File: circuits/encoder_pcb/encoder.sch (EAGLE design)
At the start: 15 parts, among them U1 MPU-6050, U2 DS18B20, X1 0.5G-WTX-NPH

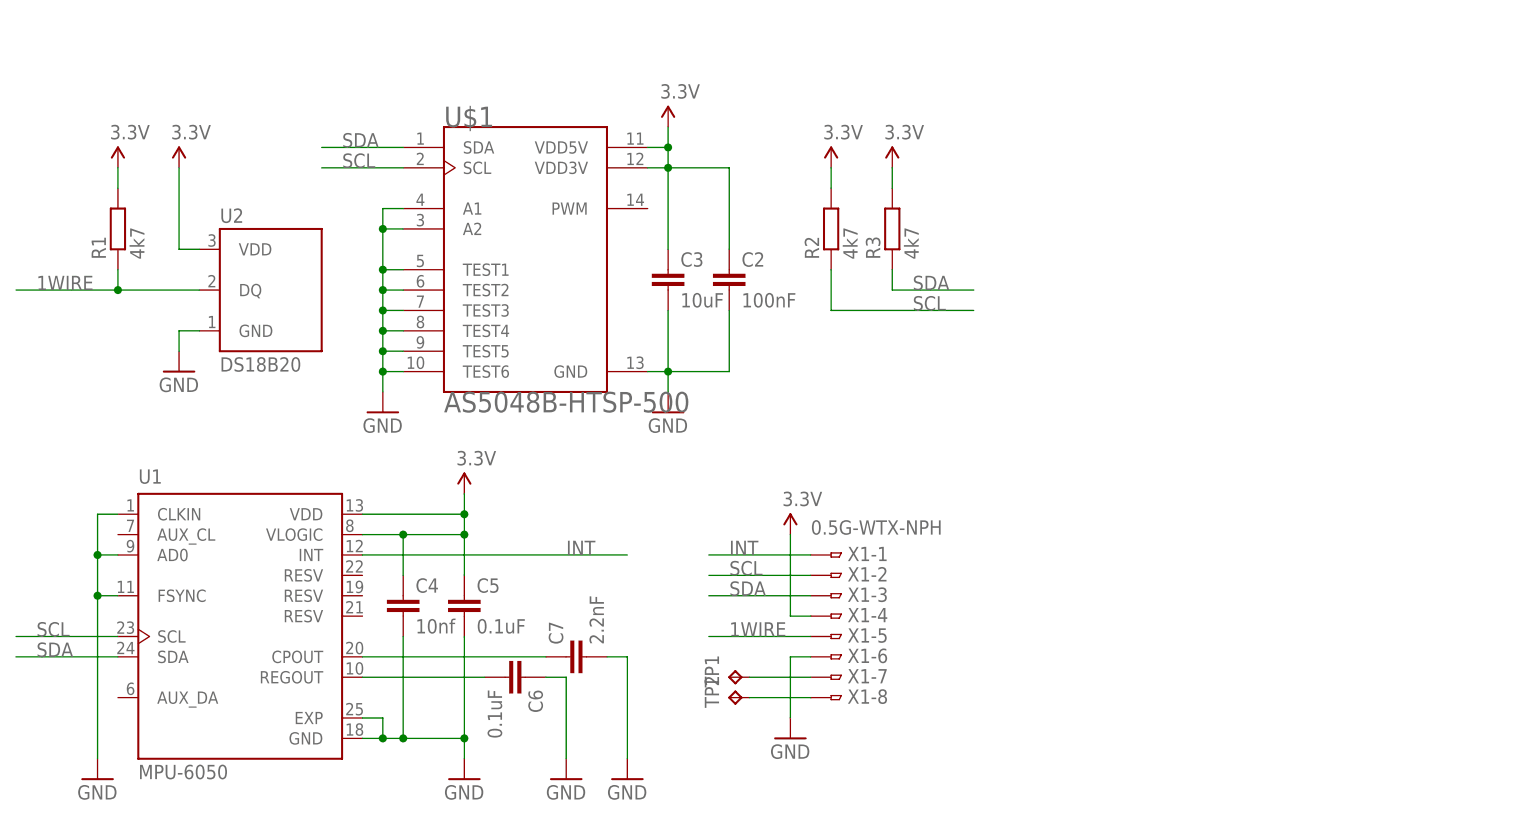
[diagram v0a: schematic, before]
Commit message: Updated encoder PCB - UNTESTED
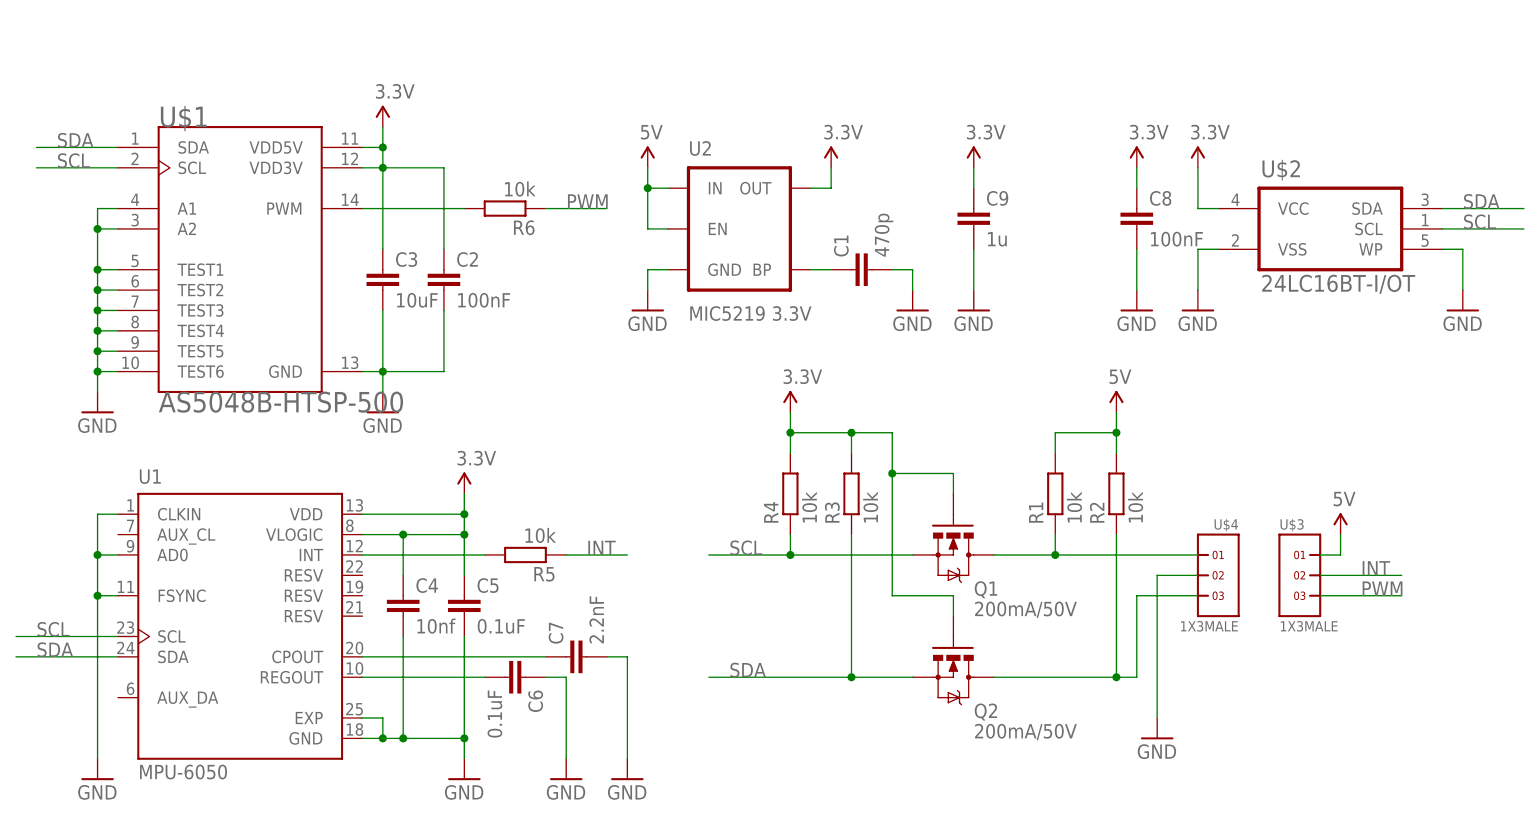
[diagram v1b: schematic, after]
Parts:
- removed TP1, TP2: TPB1,27, testpad:TPB1,27
- removed X1: 0.5G-WTX-NPH, FPC_connector_0.5G-WTX-nP:0.5G-WTX-NPH
- added C1: 470p, rcl:C-EUC0402K
- added C8: 100nF, rcl:C-EUC0402K
- added C9: 1u, rcl:C-EUC0402K
- added Q1, Q2: 200mA/50V, SparkFun-DiscreteSemi:MOSFET-NCHANNELBSS138
- added R4, R5, R6: 10k, rcl:R-EU_R0402
- added U$2: 24LC16BT-I/OT, 24LC16BT-I_OT:24LC16BT-I/OT
- added U$3, U$4: 1X3MALE, headers(.05in):1X3MALE
- R1, R2, R3: value 4k7 -> 10k
- U2: value DS18B20 -> MIC5219 3.3V; device SparkFun-Sensors:DS18B20 -> SparkFun-PowerIC:V_REG_MIC52193.3V
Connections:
- removed net 1WIRE: R1.1, U2.DQ, X1-5.1
- new net 5V: R1.2, R2.2, U$3.1, U2.EN, U2.IN
- new net N$5: R6.2, U$1.PWM
- new net N$6: Q1.D, R1.1, U$4.1
- new net N$7: Q2.D, R2.1, U$4.3
- new net PWM: R6.1, U$3.3
- net 3.3V: now also C8.1, C9.1, Q1.G, Q2.G, R4.2, U$2.VCC, U2.OUT; no longer R1.2, R2.2, U2.VDD, X1-4.1
- net GND: now also C1.2, C8.2, C9.2, U$2.VSS, U$2.WP, U$4.2; no longer X1-6.1
- net INT: now also R5.1, U$3.2; no longer U1.INT, X1-1.1
- net N$1: now also C1.1, U2.BP; no longer TP1.TP, X1-7.1
- net N$3: now also R5.2, U1.INT; no longer TP2.TP, X1-8.1
- net SCL: now also Q1.S, R4.1, U$2.SCL; no longer R2.1, X1-2.1
- net SDA: now also Q2.S, U$2.SDA; no longer X1-3.1
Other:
- moved on the sheet: C2, C3, R1, R2, R3, U$1

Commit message: Updated encoder board - UNTESTED
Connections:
- net N$6 renamed SCL_
- net N$7 renamed SDA_
- net 5V: now also U$3.3; no longer U$3.1
- net INT: now also U$3.1; no longer U$3.2
- net PWM: now also U$3.2; no longer U$3.3
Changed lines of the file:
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@@
 <net name="INT" class="0">
-<segment>
-<pinref part="U$3" gate="G$1" pin="2"/>
-<wire x1="127" y1="58.42" x2="137.16" y2="58.42" width="0.1524" layer="91"/>
-<label x="132.08" y="58.42" size="1.778" layer="95"/>
-</segment>
 <segment>
 <pinref part="R5" gate="G$1" pin="1"/>
 <wire x1="33.02" y1="60.96" x2="40.64" y2="60.96" width="0.1524" layer="91"/>
 <label x="35.56" y="60.96" size="1.778" layer="95"/>
+</segment>
+<segment>
+<pinref part="U$3" gate="G$1" pin="1"/>
+<wire x1="127" y1="60.96" x2="139.7" y2="60.96" width="0.1524" layer="91"/>
+<label x="132.08" y="60.96" size="1.778" layer="95"/>
 </segment>
 </net>
@@
 <net name="PWM" class="0">
 <segment>
-<pinref part="U$3" gate="G$1" pin="3"/>
-<wire x1="127" y1="55.88" x2="137.16" y2="55.88" width="0.1524" layer="91"/>
-<label x="132.08" y="55.88" size="1.778" layer="95"/>
-</segment>
-<segment>
 <pinref part="R6" gate="G$1" pin="1"/>
 <wire x1="30.48" y1="104.14" x2="38.1" y2="104.14" width="0.1524" layer="91"/>
 <label x="33.02" y="104.14" size="1.778" layer="95"/>
+</segment>
+<segment>
+<pinref part="U$3" gate="G$1" pin="2"/>
+<wire x1="127" y1="58.42" x2="139.7" y2="58.42" width="0.1524" layer="91"/>
+<label x="132.08" y="58.42" size="1.778" layer="95"/>
 </segment>
 </net>
@@
 </segment>
 <segment>
-<pinref part="U$3" gate="G$1" pin="1"/>
+<pinref part="U$3" gate="G$1" pin="3"/>
 <pinref part="SUPPLY2" gate="G$1" pin="5V"/>
-<wire x1="127" y1="60.96" x2="129.54" y2="60.96" width="0.1524" layer="91"/>
-<wire x1="129.54" y1="60.96" x2="129.54" y2="63.5" width="0.1524" layer="91"/>
+<wire x1="127" y1="55.88" x2="129.54" y2="55.88" width="0.1524" layer="91"/>
+<wire x1="129.54" y1="55.88" x2="129.54" y2="63.5" width="0.1524" layer="91"/>
 </segment>
 </net>
@@
 </segment>
 </net>
-<net name="N$6" class="0">
+<net name="SCL_" class="0">
 <segment>
 <pinref part="Q1" gate="G$1" pin="D"/>
@@
 <pinref part="R1" gate="G$1" pin="1"/>
 <wire x1="93.98" y1="63.5" x2="93.98" y2="60.96" width="0.1524" layer="91"/>
+<wire x1="93.98" y1="60.96" x2="111.76" y2="60.96" width="0.1524" layer="91"/>
+<junction x="93.98" y="60.96"/>
 <pinref part="U$4" gate="G$1" pin="1"/>
-<wire x1="111.76" y1="60.96" x2="93.98" y2="60.96" width="0.1524" layer="91"/>
-<junction x="93.98" y="60.96"/>
 </segment>
 </net>
-<net name="N$7" class="0">
+<net name="SDA_" class="0">
 <segment>
 <pinref part="Q2" gate="G$1" pin="D"/>

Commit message: Updated encoder to revision 1 - UNTESTED
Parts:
- removed R6: 10k, rcl:R-EU_R0402
- removed U$3, U$4: 1X3MALE, headers(.05in):1X3MALE
- added U$5: 1X5, headers(.05in):1X5
- renumbered U$1 to U4, U$2 to U3
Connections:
- removed net N$5: R6.2, U4.PWM
- removed net PWM: R6.1, U$3.2
- net 5V: now also U$5.2; no longer U$3.3
- net GND: now also U$5.4; no longer U$4.2
- net INT: now also U$5.1; no longer U$3.1
- net SCL_: now also U$5.5; no longer U$4.1
- net SDA_: now also U$5.3; no longer U$4.3

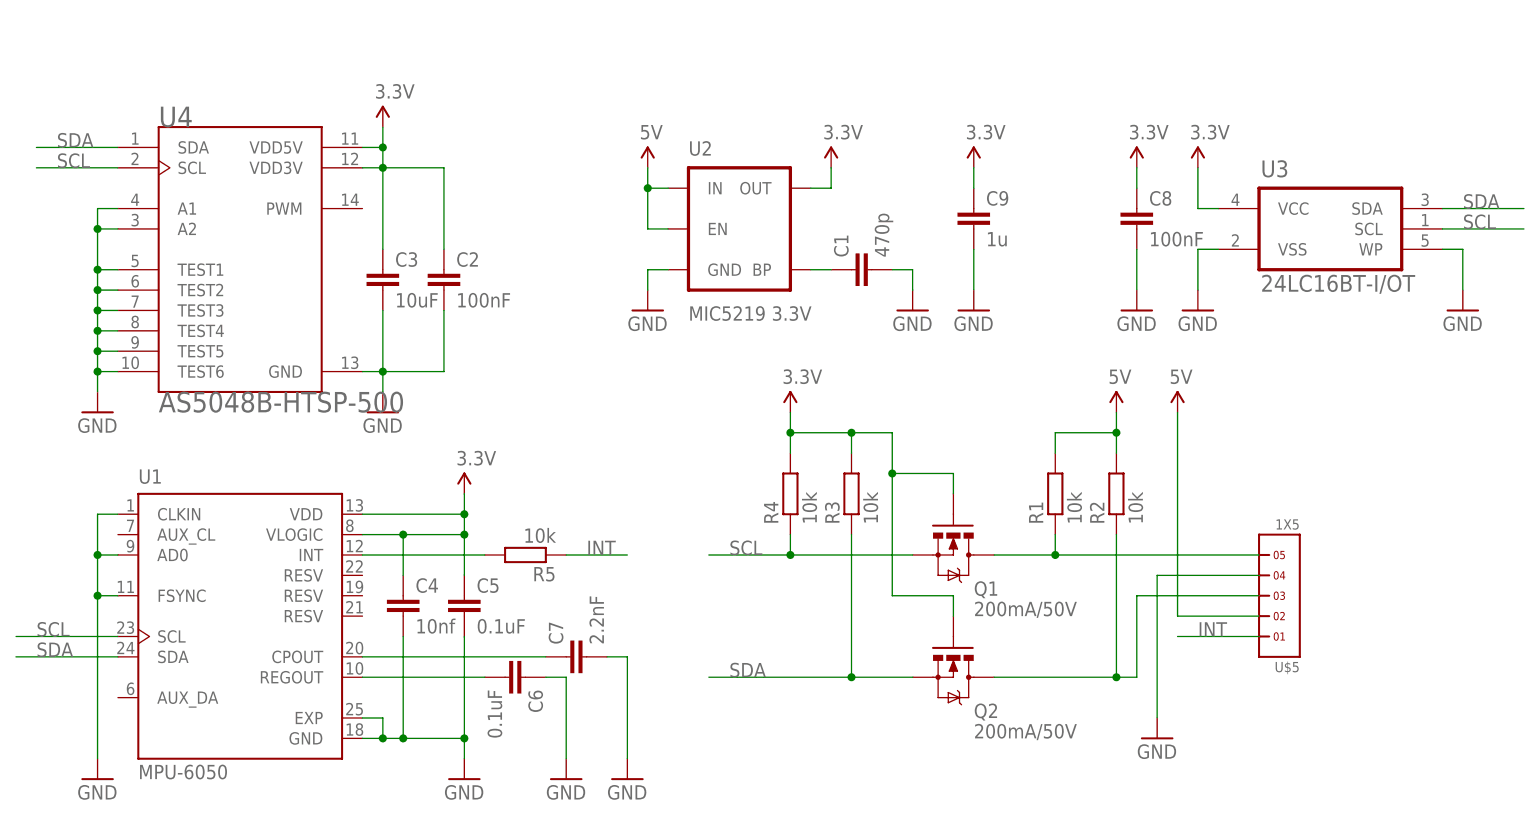
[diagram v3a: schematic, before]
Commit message: Updated encoder PCB - Tested and working
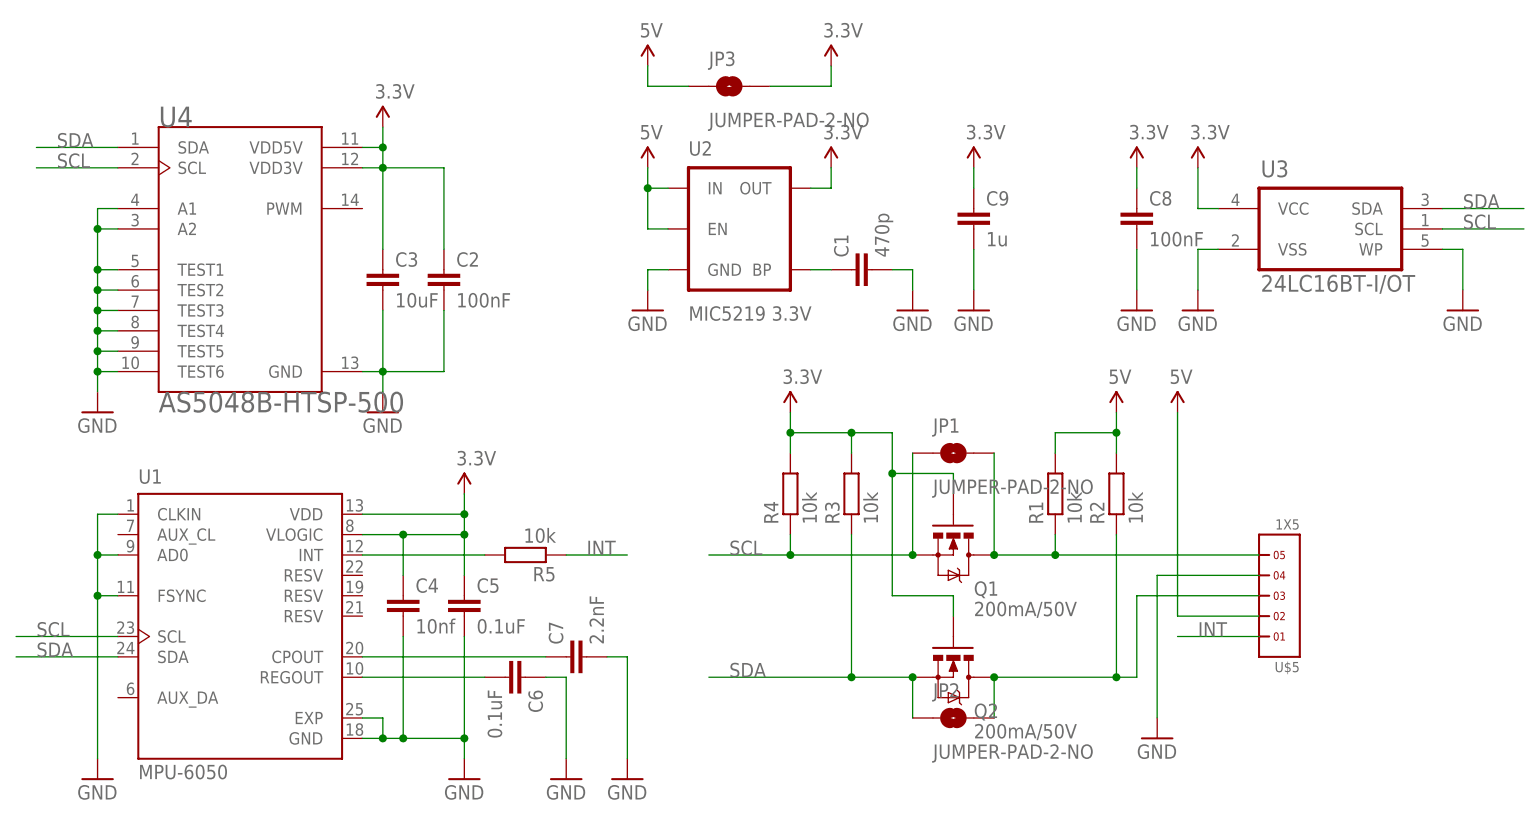
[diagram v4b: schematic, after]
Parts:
- added JP1, JP2, JP3: JUMPER-PAD-2-NO, SparkFun-Passives:JUMPER-PAD-2-NO
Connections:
- net 3.3V: now also JP3.2
- net 5V: now also JP3.1
- net SCL: now also JP1.1
- net SCL_: now also JP1.2
- net SDA: now also JP2.1
- net SDA_: now also JP2.2
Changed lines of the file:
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@@
 <part name="U$5" library="headers(.05in)" deviceset="1X5" device=""/>
 <part name="SUPPLY11" library="SparkFun-Aesthetics" deviceset="5V" device=""/>
+<part name="JP1" library="SparkFun-Passives" deviceset="JUMPER-PAD-2-NO" device=""/>
+<part name="JP2" library="SparkFun-Passives" deviceset="JUMPER-PAD-2-NO" device=""/>
+<part name="JP3" library="SparkFun-Passives" deviceset="JUMPER-PAD-2-NO" device=""/>
+<part name="SUPPLY2" library="SparkFun-Aesthetics" deviceset="5V" device=""/>
+<part name="SUPPLY12" library="SparkFun-Aesthetics" deviceset="3.3V" device=""/>
 </parts>
 <sheets>
@@
 <instance part="U$5" gate="G$1" x="121.92" y="55.88" rot="R180"/>
 <instance part="SUPPLY11" gate="G$1" x="109.22" y="78.74"/>
+<instance part="JP1" gate="G$1" x="81.28" y="73.66"/>
+<instance part="JP2" gate="G$1" x="81.28" y="40.64"/>
+<instance part="JP3" gate="G$1" x="53.34" y="119.38"/>
+<instance part="SUPPLY2" gate="G$1" x="43.18" y="121.92"/>
+<instance part="SUPPLY12" gate="G$1" x="66.04" y="121.92"/>
 </instances>
 <busses>
@@
 <pinref part="SUPPLY10" gate="G$1" pin="3.3V"/>
 <wire x1="83.82" y1="109.22" x2="83.82" y2="106.68" width="0.1524" layer="91"/>
+</segment>
+<segment>
+<pinref part="JP3" gate="G$1" pin="2"/>
+<pinref part="SUPPLY12" gate="G$1" pin="3.3V"/>
+<wire x1="58.42" y1="119.38" x2="66.04" y2="119.38" width="0.1524" layer="91"/>
+<wire x1="66.04" y1="119.38" x2="66.04" y2="121.92" width="0.1524" layer="91"/>
 </segment>
 </net>
@@
 <junction x="68.58" y="45.72"/>
 <label x="53.34" y="45.72" size="1.778" layer="95"/>
+<pinref part="JP2" gate="G$1" pin="1"/>
+<wire x1="76.2" y1="40.64" x2="76.2" y2="45.72" width="0.1524" layer="91"/>
+<junction x="76.2" y="45.72"/>
 </segment>
 </net>
@@
 <junction x="60.96" y="60.96"/>
 <label x="53.34" y="60.96" size="1.778" layer="95"/>
+<pinref part="JP1" gate="G$1" pin="1"/>
+<wire x1="76.2" y1="73.66" x2="76.2" y2="60.96" width="0.1524" layer="91"/>
+<junction x="76.2" y="60.96"/>
 </segment>
 </net>
@@
 <pinref part="U$5" gate="G$1" pin="2"/>
 </segment>
+<segment>
+<pinref part="JP3" gate="G$1" pin="1"/>
+<pinref part="SUPPLY2" gate="G$1" pin="5V"/>
+<wire x1="48.26" y1="119.38" x2="43.18" y2="119.38" width="0.1524" layer="91"/>
+<wire x1="43.18" y1="119.38" x2="43.18" y2="121.92" width="0.1524" layer="91"/>
+</segment>
 </net>
 <net name="N$1" class="0">
@@
 <junction x="93.98" y="60.96"/>
 <pinref part="U$5" gate="G$1" pin="5"/>
+<pinref part="JP1" gate="G$1" pin="2"/>
+<wire x1="86.36" y1="73.66" x2="86.36" y2="60.96" width="0.1524" layer="91"/>
+<junction x="86.36" y="60.96"/>
 </segment>
 </net>
@@
 <wire x1="119.38" y1="55.88" x2="104.14" y2="55.88" width="0.1524" layer="91"/>
 <pinref part="U$5" gate="G$1" pin="3"/>
-</segment>
-</net>
+<pinref part="JP2" gate="G$1" pin="2"/>
+<wire x1="86.36" y1="40.64" x2="86.36" y2="45.72" width="0.1524" layer="91"/>
+<junction x="86.36" y="45.72"/>
+</segment>
+</net>
